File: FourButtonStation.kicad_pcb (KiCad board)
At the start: 2 copper layers, 106 x 65 mm, 89 parts, among them J1 AC IN, J10 AC IN, J2 External 3V, J3 UART, J4 ADC, J5 Conn_WallSocket, J6 USB_B_Micro, J7 Conn_WallSocket, J8 Conn_WallSocket, J9 Conn_WallSocket, K1 G5LE-1, K2 G5LE-1, K3 G5LE-1, K4 G5LE-1, Q1 MMBT3904, Q3 MMBT3904, SW1 POWER, SW2 RST, SW5 Mode, U1 CH340C, U10 SM4007PL, U11 D882_C9634, U13 AMS1117-3_3, U2 radio-receiver, U3 ESP-07, U4 SM4007PL, U5 D882_C9634, U6 SM4007PL, U7 D882_C9634, U8 SM4007PL, U9 D882_C9634

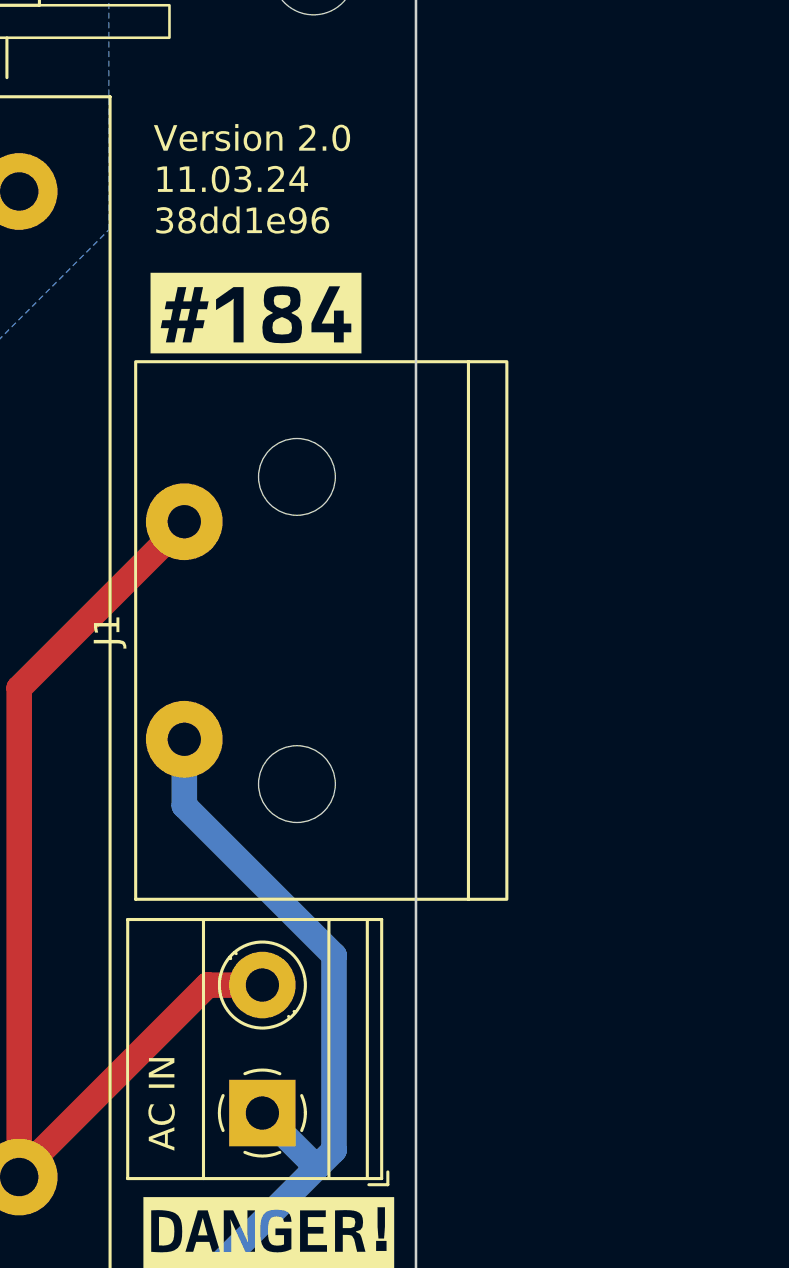
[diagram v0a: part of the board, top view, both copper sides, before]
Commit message: Add another C8 Power entry AC plug as an option
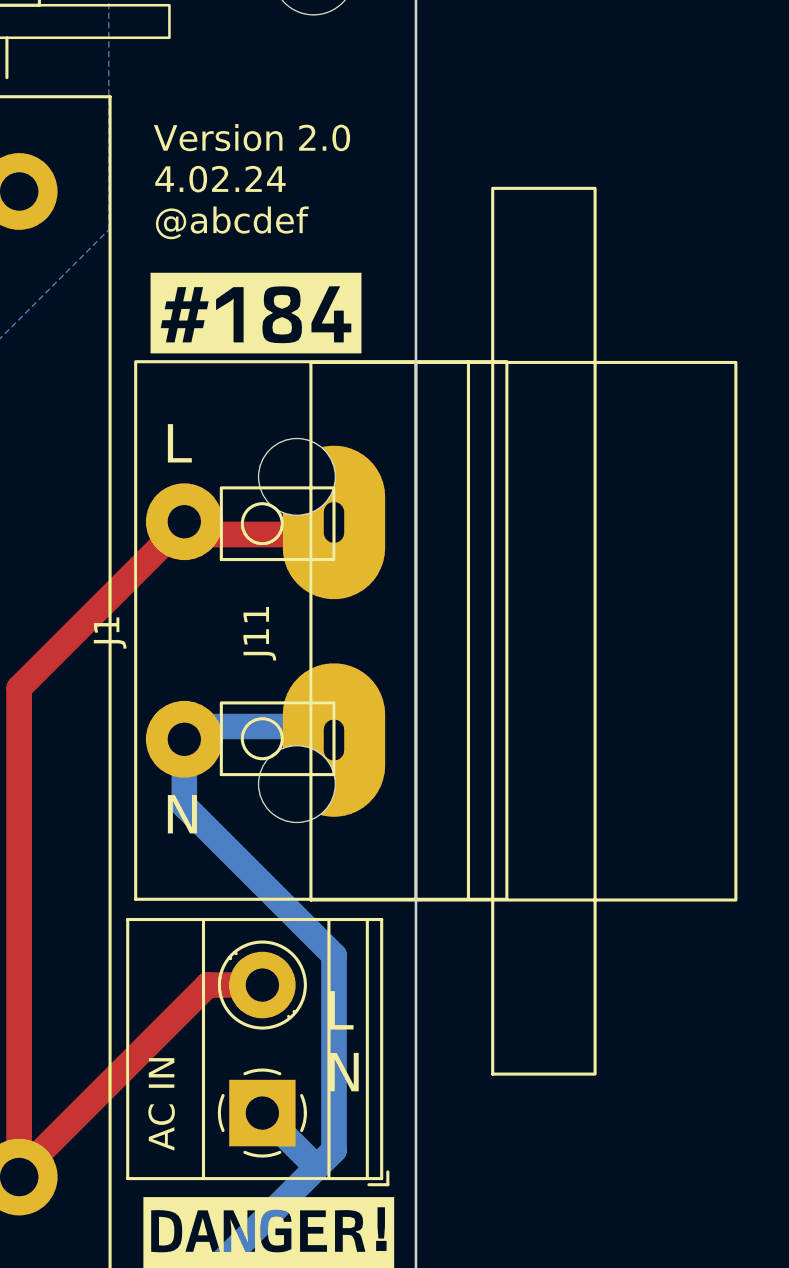
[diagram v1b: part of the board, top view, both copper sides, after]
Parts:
- removed SYM1 (x7): SYM_Flash_XLarge, Symbol:Symbol_HighVoltage_Type2_CopperTop_VerySmall
- removed Sym2: github.com/besi/four-button-station, Symbol:OSHW-Symbol_6.7x6mm_SilkScreen
- added J11: AC IN, c8-inlet:c8-inlet, F.Cu at (120.0, 119.4)
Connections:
- PS1 pad 3: GND -> unconnected-(PS1--Vo-Pad3)
- U11 pad 3: GND -> unconnected-(U11-E-Pad3)
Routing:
- net /Phase: track 212.6 -> 218.9 mm
- net /AC_FUSE: track 35.7 -> 41.2 mm
- net GND: track 49.9 -> 47.7 mm, vias 22 -> 21
- net unconnected-(U11-E-Pad3): track 0.00 -> 2.18 mm, vias 0 -> 1
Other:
- board text added: "L N"
- board text added: "Version 2.0 4.02.24 @abcdef"
- board text removed: "Version 2.0 11.03.24 38dd1e96"

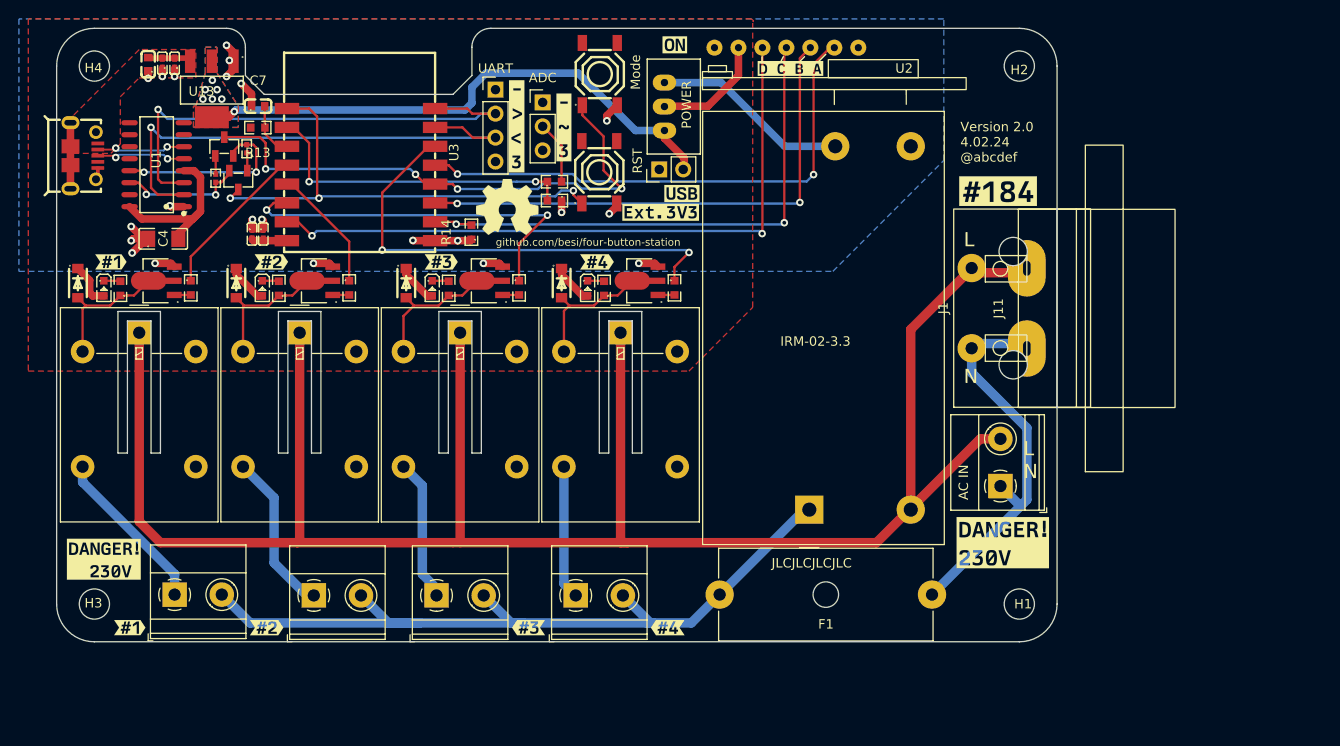
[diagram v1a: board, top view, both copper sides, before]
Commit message: Fix erroneously matched 1k resistors
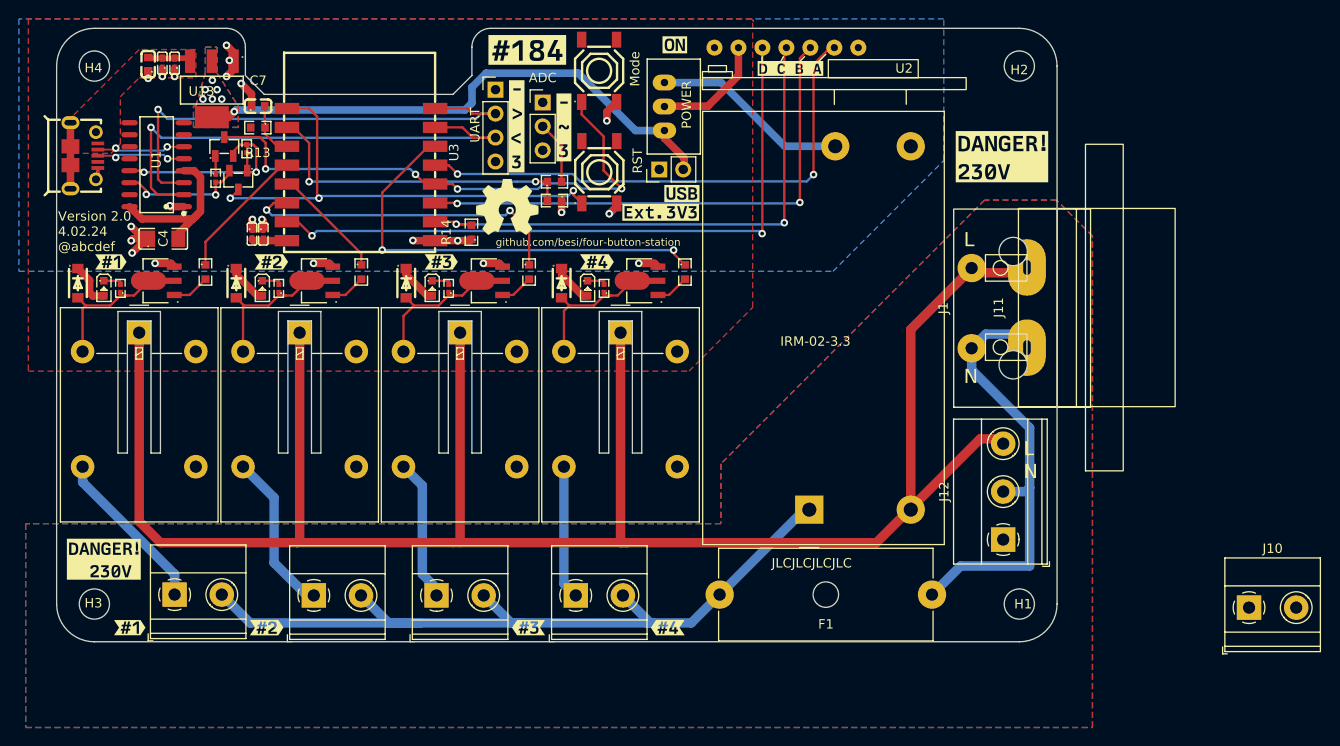
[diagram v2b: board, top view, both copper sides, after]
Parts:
- added J12: AC IN, TerminalBlock_Phoenix:TerminalBlock_Phoenix_MKDS-1,5-3-5.08_1x03_P5.08mm_Horizontal, F.Cu at (117.5, 143.9)
- R4, R5, R7, R9: footprint jlc_footprints:R0603 -> jlc_footprints:R0402
- moved kibuzzard-65EDF79E 52.1 mm to (67.1, 92.0)
- moved kibuzzard-65EE278E 40.9 mm to (117.4, 103.4)
- moved J10 29.3 mm to (143.6, 151.1), turned to 0 degrees
- moved R1 2.29 mm to (33.0, 115.6)
- moved R6 2.11 mm to (49.5, 115.6)
- moved R10 2.01 mm to (83.8, 115.6)
- moved R8 1.99 mm to (67.3, 115.6)
- moved SW5 0.35 mm to (74.7, 94.3)
- moved J11 0.09 mm to (120.1, 119.3)
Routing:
- net /AC_FUSE: track 41.2 -> 47.3 mm
- net Relay3: track 40.6 -> 35.3 mm
- net Relay4: track 50.0 -> 46.7 mm
- net Relay1: track 16.8 -> 14.4 mm
- net Net-(U5-B): track 1.75 -> 4.00 mm
- net Net-(U7-B): track 1.75 -> 3.72 mm
- net Net-(U11-B): track 1.75 -> 3.55 mm
- net Net-(U9-B): track 1.75 -> 3.50 mm
- net Relay2: track 13.3 -> 12.2 mm
- net /Phase: track 218.9 -> 218.2 mm
- added copper zone on B.Cu, net Earth
- added copper zone on F.Cu, net Earth

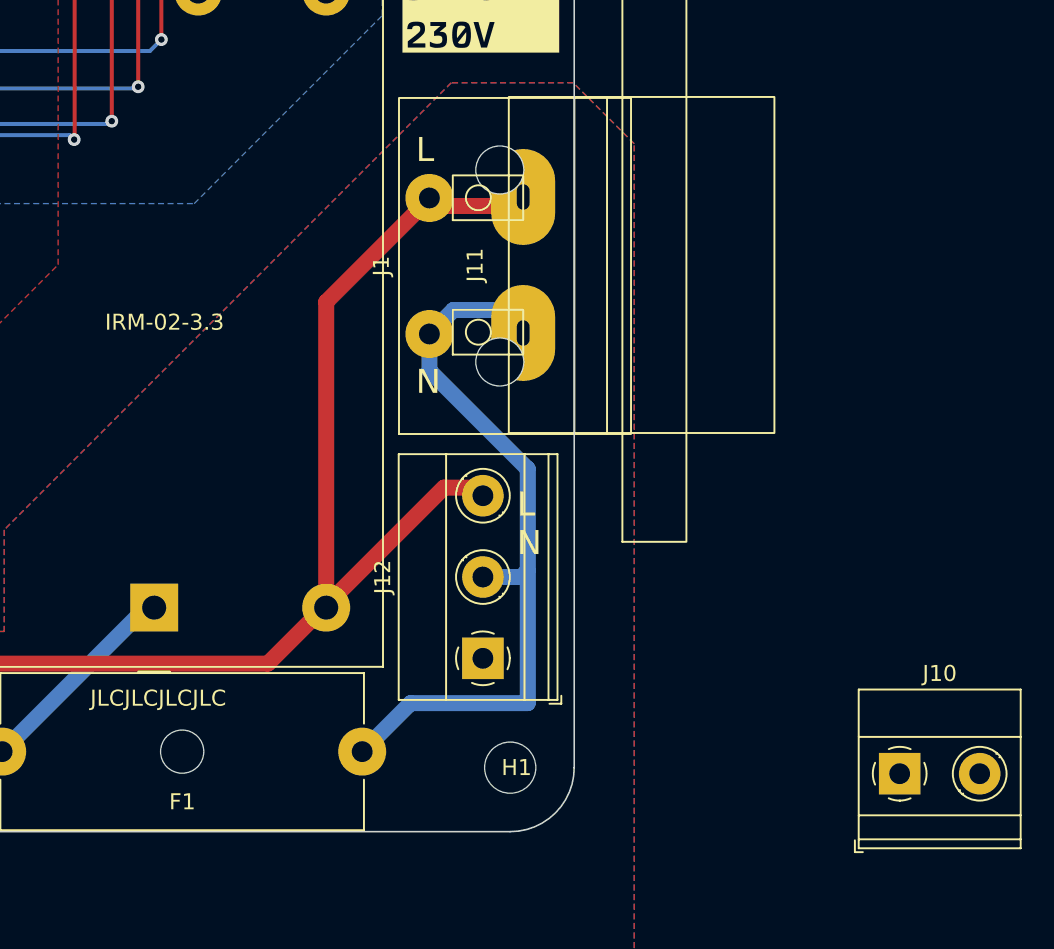
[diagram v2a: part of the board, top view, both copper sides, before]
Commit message: Rule checks and Silkscreen
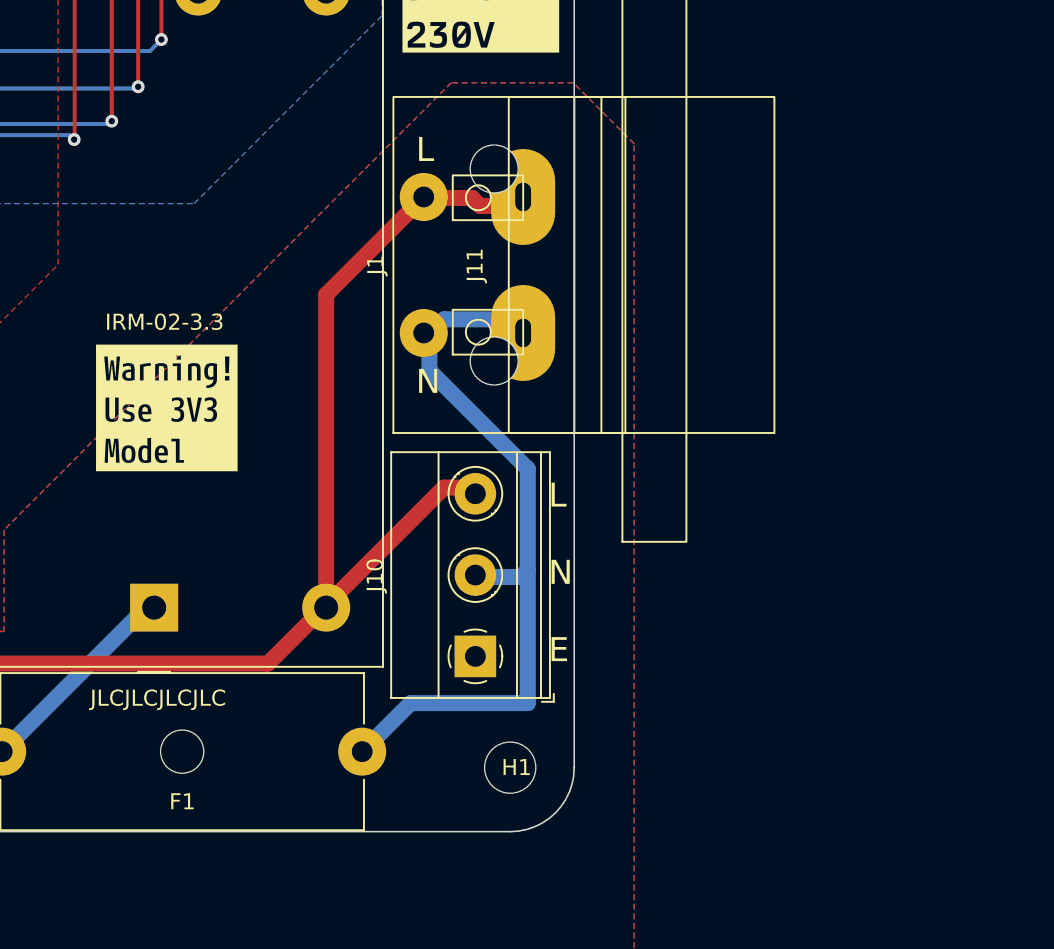
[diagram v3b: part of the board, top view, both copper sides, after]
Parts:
- removed J12: AC IN, TerminalBlock_Phoenix:TerminalBlock_Phoenix_MKDS-1,5-3-5.08_1x03_P5.08mm_Horizontal
- added kibuzzard-67A2052C: G***, kibuzzard-67A2052C, F.Cu at (97.8, 128.3)
- J10: footprint TerminalBlock_Phoenix:TerminalBlock_Phoenix_MKDS-1,5-2_1x02_P5.00mm_Horizontal -> TerminalBlock_Phoenix:TerminalBlock_Phoenix_MKDS-1,5-3-5.08_1x03_P5.08mm_Horizontal
- moved J10 27.5 mm to (117.1, 143.8), turned to 90 degrees
- moved J1 0.36 mm to (113.8, 119.3)
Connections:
- J10 pad 1: /AC_FUSE -> Earth
- J10 pad 2: /Phase -> /AC_FUSE
- PS1 pad 3: unconnected-(PS1--Vo-Pad3) -> GND
- U11 pad 3: unconnected-(U11-E-Pad3) -> GND
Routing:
- net unconnected-(U11-E-Pad3): track 2.18 -> 0.00 mm, vias 1 -> 0
- net GND: track 48.1 -> 50.2 mm, vias 21 -> 22
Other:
- board text added: "L N E"

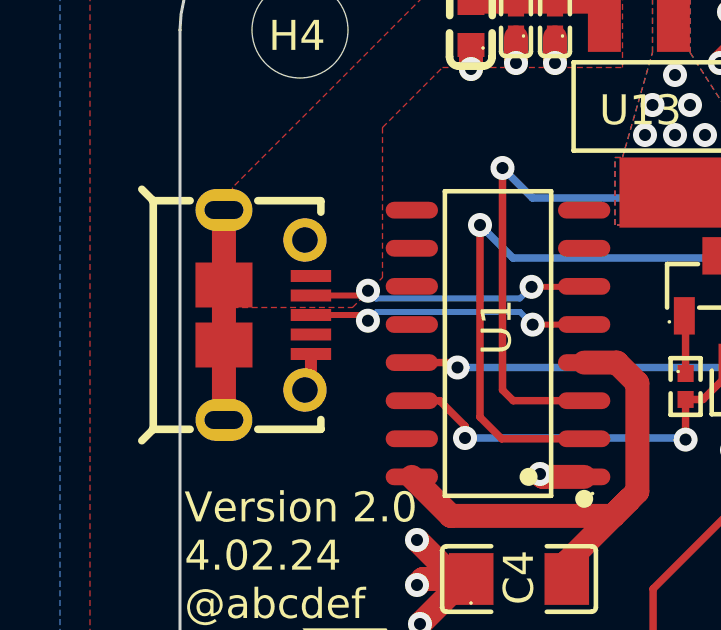
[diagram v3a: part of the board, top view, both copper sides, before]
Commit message: Replace USB connector due to short fall
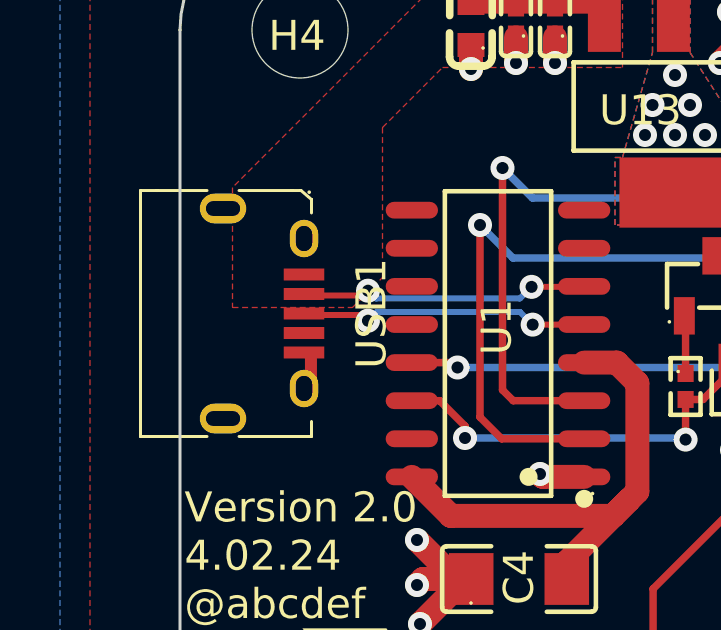
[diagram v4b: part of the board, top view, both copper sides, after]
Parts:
- removed J6: USB_B_Micro, jlc_footprints:MICRO-USB-SMD_1050171001
- added USB1: 10118194-0001LF, jlc_footprints:MICRO-USB-SMD_10118194-0001LF, F.Cu at (20.0, 103.2)
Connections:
- U1 pad 5: /UD_P -> Net-(U1-UD+)
- U1 pad 6: /UD_N -> Net-(U1-UD-)
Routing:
- net Net-(U1-UD+): track 0.00 -> 9.48 mm, vias 0 -> 2
- net /UD_P: track 9.48 -> 0.00 mm, vias 2 -> 0
- net Net-(U1-UD-): track 0.00 -> 9.45 mm, vias 0 -> 2
- net /UD_N: track 9.45 -> 0.00 mm, vias 2 -> 0
- net GND: track 50.2 -> 42.5 mm
